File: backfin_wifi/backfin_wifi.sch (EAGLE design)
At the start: 22 parts

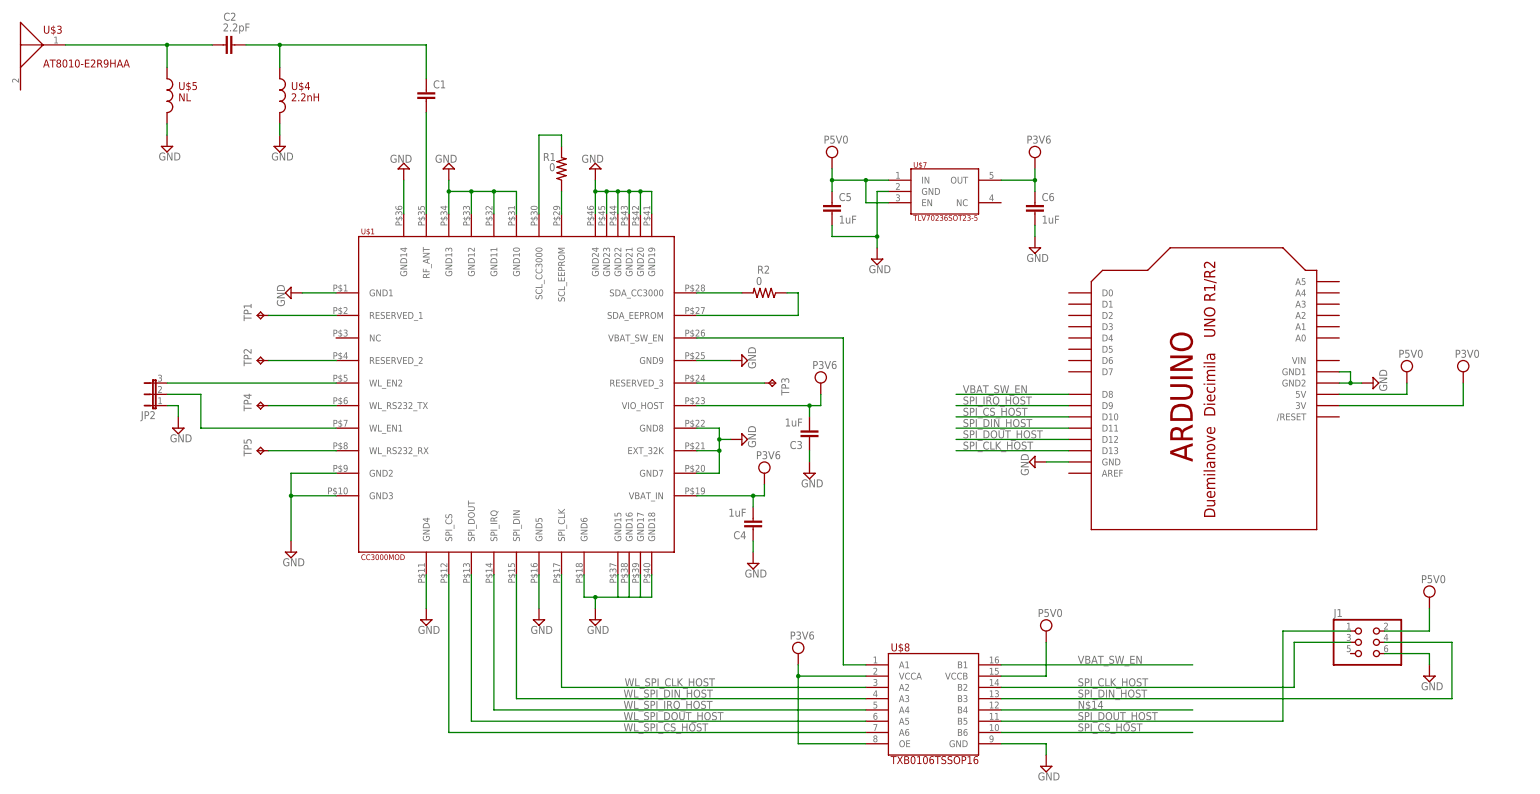
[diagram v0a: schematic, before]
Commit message: Added push button and LED
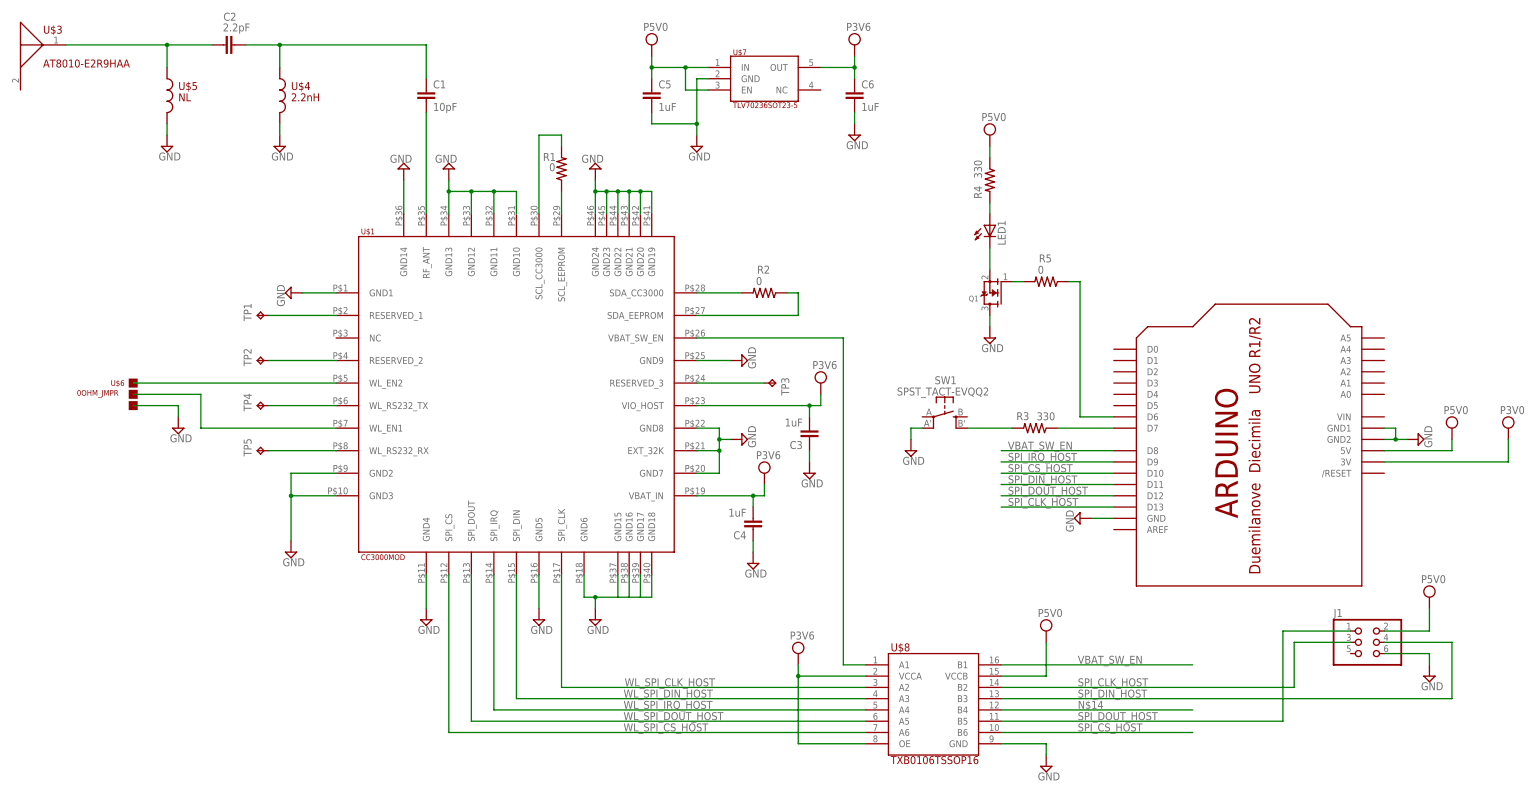
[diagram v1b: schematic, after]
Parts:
- removed JP2: (no value), jumper:JP2E
- added LED1: (no value), adafruit:LEDCHIPLED_1206
- added Q1: (no value), adafruit:MOSFET-NREFLOW
- added R3, R4: 330, resistor:R-US_R1005
- added R5: 0, resistor:R-US_R1005
- added SW1: SPST_TACT-EVQQ2, adafruit:SPST_TACT-EVQQ2
- added U$6: 0OHM_JMPR, custom:0OHM_JMPR
- C1: value (none) -> 10pF
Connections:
- new net N$17: R3.1, U$2.D7
- new net N$18: R3.2, SW1.S1
- new net N$19: R5.1, U$2.D6
- new net N$20: LED1.C, Q1.S
- new net N$21: LED1.A, R4.2
- new net N$22: Q1.G, R5.2
- new net SPI_IRQ_HOST: U$2.D9
- net GND: now also Q1.D, SW1.P1; no longer JP2.1
- net N$1: no longer JP2.2
- net N$2: no longer JP2.3
- net SPI_CLK_HOST: now also U$2.D13
- net SPI_CS_HOST: now also U$2.D10
- net SPI_DIN_HOST: now also U$2.D11
- net SPI_DOUT_HOST: now also U$2.D12
- net VBAT_SW_EN: now also U$2.D8
- net VCC: now also R4.1
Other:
- moved on the sheet: C5, C6, U$7

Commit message: more work...
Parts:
- removed U$6: 0OHM_JMPR, custom:0OHM_JMPR
- added R6, R7: 0, resistor:R-US_R1005
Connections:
- removed net VCC: C3.2, C4.2, C5.1, C6.1, J1.2, R4.1, U$1.VBAT_IN, U$1.VIO_HOST, U$2.3V, U$2.5V, U$7.EN, U$7.IN, U$7.OUT, U$8.OE, U$8.VCCA, U$8.VCCB
- new net +4.1V: C3.2, C4.2, C6.1, U$1.VBAT_IN, U$1.VIO_HOST, U$7.OUT, U$8.OE, U$8.VCCA
- new net +5V: C5.1, J1.2, R4.1, U$2.5V, U$7.EN, U$7.IN, U$8.VCCB
- net GND: now also R7.2
- net N$1: now also R6.1
- net N$2: now also R6.2, R7.1
